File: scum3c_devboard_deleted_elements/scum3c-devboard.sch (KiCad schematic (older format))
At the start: 9 parts, among them U9AB1 MPU-9250

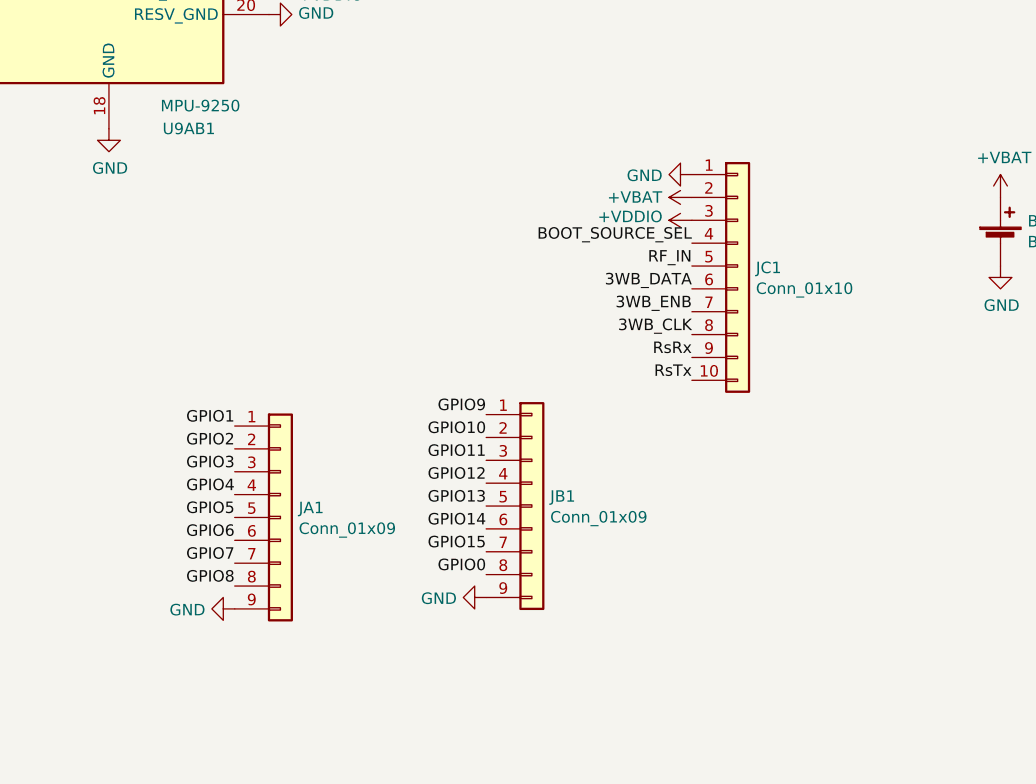
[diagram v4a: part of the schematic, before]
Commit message: shrink to 30mm square
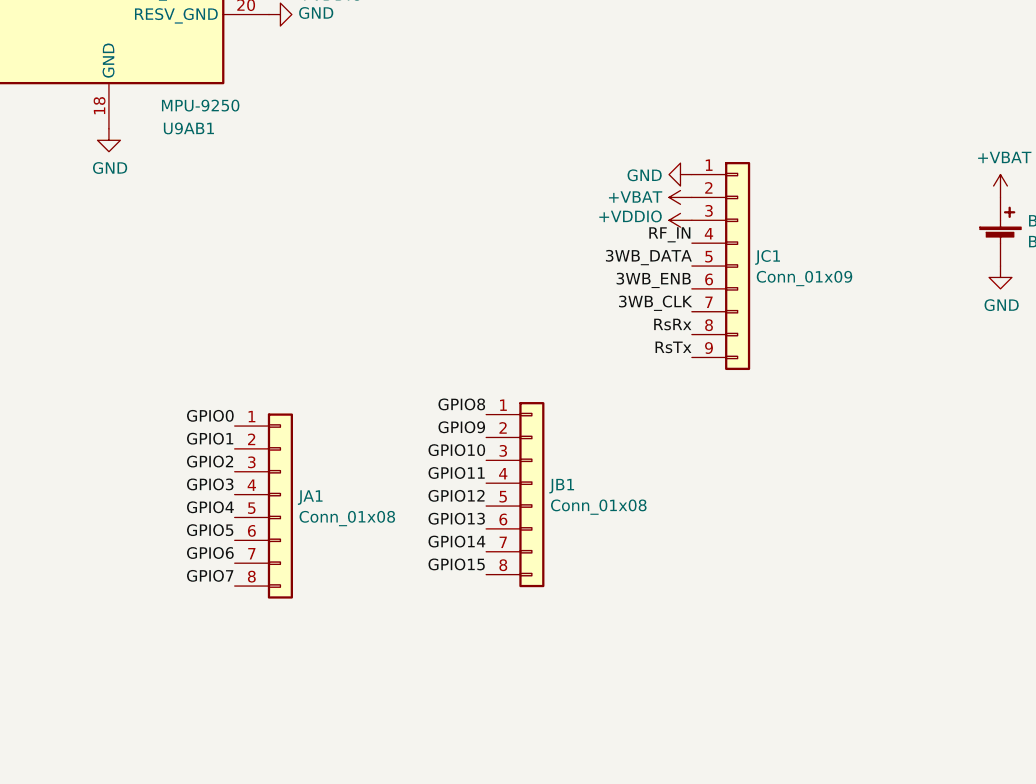
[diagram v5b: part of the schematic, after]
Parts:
- removed JA1, JB1: Conn_01x09, Connector_PinHeader_2.54mm:PinHeader_1x09_P2.54mm_Vertical, symbol Connector_Generic:Conn_01x09
- removed JC1: Conn_01x10, Connector_PinHeader_2.54mm:PinHeader_1x10_P2.54mm_Vertical, symbol Connector_Generic:Conn_01x10
- added JA1, JB1: Conn_01x08, Connector_PinHeader_2.54mm:PinHeader_1x08_P2.54mm_Vertical, symbol Connector_Generic:Conn_01x08
- added JC1: Conn_01x09, Connector_PinHeader_2.54mm:PinHeader_1x09_P2.54mm_Vertical, symbol Connector_Generic:Conn_01x09
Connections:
- net +VBAT: now also JC1.2 (Pin_2)
- net +VDDIO: now also JC1.3 (Pin_3)
- net 3WB_CLK: now also JC1.7 (Pin_7)
- net 3WB_DATA: now also JC1.5 (Pin_5)
- net 3WB_ENB: now also JC1.6 (Pin_6)
- net GND: now also JC1.1 (Pin_1)
- net GPIO0: now also JA1.1 (Pin_1)
- net GPIO1: now also JA1.2 (Pin_2)
- net GPIO10: now also JB1.3 (Pin_3)
- net GPIO11: now also JB1.4 (Pin_4)
- net GPIO12: now also JB1.5 (Pin_5)
- net GPIO13: now also JB1.6 (Pin_6)
- net GPIO14: now also JB1.7 (Pin_7)
- net GPIO15: now also JB1.8 (Pin_8)
- net GPIO2: now also JA1.3 (Pin_3)
- net GPIO3: now also JA1.4 (Pin_4)
- net GPIO4: now also JA1.5 (Pin_5)
- net GPIO5: now also JA1.6 (Pin_6)
- net GPIO6: now also JA1.7 (Pin_7)
- net GPIO7: now also JA1.8 (Pin_8)
- net GPIO8: now also JB1.1 (Pin_1)
- net GPIO9: now also JB1.2 (Pin_2)
- net RF_IN: now also JC1.4 (Pin_4)
- net RsRx: now also JC1.8 (Pin_8)
- net RsTx: now also JC1.9 (Pin_9)
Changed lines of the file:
@@
 	1    0    0    -1
 $EndComp
+Text Label 3550 4500 2    50   ~ 0
+GPIO10
+Text Label 3550 4700 2    50   ~ 0
+GPIO12
+Text Label 3550 4900 2    50   ~ 0
+GPIO14
+Text Label 3550 5000 2    50   ~ 0
+GPIO15
 Text Label 3550 4400 2    50   ~ 0
-GPIO10
+GPIO9
+Text Label 2450 4350 2    50   ~ 0
+GPIO0
+Text Label 3550 4800 2    50   ~ 0
+GPIO13
 Text Label 3550 4600 2    50   ~ 0
-GPIO12
-Text Label 3550 4800 2    50   ~ 0
-GPIO14
-Text Label 3550 4900 2    50   ~ 0
-GPIO15
-$Comp
-L power:GND #PWR0111
-U 1 1 5F3EC8B2
-P 2450 5150
-F 0 "#PWR0111" H 2450 4900 50  0001 C CNN
-F 1 "GND" V 2455 5022 50  0000 R CNN
-F 2 "" H 2450 5150 50  0001 C CNN
-F 3 "" H 2450 5150 50  0001 C CNN
-	1    2450 5150
-	0    1    1    0
-$EndComp
-Text Label 3550 4300 2    50   ~ 0
-GPIO9
-Text Label 3550 5000 2    50   ~ 0
-GPIO0
-Text Label 3550 4700 2    50   ~ 0
-GPIO13
-Text Label 3550 4500 2    50   ~ 0
 GPIO11
-$Comp
-L power:GND #PWR0112
-U 1 1 5F3ED1BB
-P 3550 5100
-F 0 "#PWR0112" H 3550 4850 50  0001 C CNN
-F 1 "GND" V 3555 4972 50  0000 R CNN
-F 2 "" H 3550 5100 50  0001 C CNN
-F 3 "" H 3550 5100 50  0001 C CNN
-	1    3550 5100
-	0    1    1    0
-$EndComp
 $Comp
 L power:PWR_FLAG #FLG0101
@@
 	0    -1   -1   0
 $EndComp
-Text Label 4450 3550 2    50   ~ 0
-BOOT_SOURCE_SEL
 $Comp
 L draft1library:+VDDIO #PWR?
@@
 Text Label 9400 3250 0    50   ~ 0
 BOOT_SOURCE_SEL
-$Comp
-L Connector_Generic:Conn_01x10 JC1
-U 1 1 5F7BC634
-P 4650 3650
-F 0 "JC1" H 4730 3642 50  0000 L CNN
-F 1 "Conn_01x10" H 4730 3551 50  0000 L CNN
-F 2 "Connector_PinHeader_2.54mm:PinHeader_1x10_P2.54mm_Vertical" H 4650 3650 50  0001 C CNN
-F 3 "~" H 4650 3650 50  0001 C CNN
-	1    4650 3650
-	1    0    0    -1
-$EndComp
+Text Label 2450 4650 2    50   ~ 0
+GPIO3
+Text Label 2450 4850 2    50   ~ 0
+GPIO5
+Text Label 2450 5050 2    50   ~ 0
+GPIO7
+Text Label 2450 4450 2    50   ~ 0
+GPIO1
 Text Label 2450 4550 2    50   ~ 0
-GPIO3
+GPIO2
 Text Label 2450 4750 2    50   ~ 0
-GPIO5
+GPIO4
 Text Label 2450 4950 2    50   ~ 0
-GPIO7
-Text Label 2450 4350 2    50   ~ 0
-GPIO1
-Text Label 2450 4450 2    50   ~ 0
-GPIO2
-Text Label 2450 4650 2    50   ~ 0
-GPIO4
-Text Label 2450 4850 2    50   ~ 0
 GPIO6
-Text Label 2450 5050 2    50   ~ 0
+Text Label 3550 4300 2    50   ~ 0
 GPIO8
 Text Label 9400 1500 0    50   ~ 0
@@
 Text Label 8550 3050 2    50   ~ 0
 RsTx
-$Comp
-L Connector_Generic:Conn_01x09 JA1
-U 1 1 5F7CC956
-P 2650 4750
-F 0 "JA1" H 2730 4792 50  0000 L CNN
-F 1 "Conn_01x09" H 2730 4701 50  0000 L CNN
-F 2 "Connector_PinHeader_2.54mm:PinHeader_1x09_P2.54mm_Vertical" H 2650 4750 50  0001 C CNN
-F 3 "~" H 2650 4750 50  0001 C CNN
-	1    2650 4750
-	1    0    0    -1
-$EndComp
-$Comp
-L Connector_Generic:Conn_01x09 JB1
-U 1 1 5F7CF946
-P 3750 4700
-F 0 "JB1" H 3830 4742 50  0000 L CNN
-F 1 "Conn_01x09" H 3830 4651 50  0000 L CNN
-F 2 "Connector_PinHeader_2.54mm:PinHeader_1x09_P2.54mm_Vertical" H 3750 4700 50  0001 C CNN
-F 3 "~" H 3750 4700 50  0001 C CNN
-	1    3750 4700
-	1    0    0    -1
-$EndComp
 $Comp
 L power:GND #PWR0124
@@
 	0    1    1    0
 $EndComp
+Text Label 4450 3950 2    50   ~ 0
+RsRx
 Text Label 4450 4050 2    50   ~ 0
-RsRx
-Text Label 4450 4150 2    50   ~ 0
 RsTx
-Text Label 4450 3950 2    50   ~ 0
+Text Label 4450 3850 2    50   ~ 0
 3WB_CLK
-Text Label 4450 3850 2    50   ~ 0
+Text Label 4450 3750 2    50   ~ 0
 3WB_ENB
-Text Label 4450 3750 2    50   ~ 0
+Text Label 4450 3650 2    50   ~ 0
 3WB_DATA
-Text Label 4450 3650 2    50   ~ 0
+Text Label 4450 3550 2    50   ~ 0
 RF_IN
+$Comp
+L Connector_Generic:Conn_01x08 JA1
+U 1 1 5F7FC97F
+P 2650 4650
+F 0 "JA1" H 2730 4642 50  0000 L CNN
+F 1 "Conn_01x08" H 2730 4551 50  0000 L CNN
+F 2 "Connector_PinHeader_2.54mm:PinHeader_1x08_P2.54mm_Vertical" H 2650 4650 50  0001 C CNN
+F 3 "~" H 2650 4650 50  0001 C CNN
+	1    2650 4650
+	1    0    0    -1
+$EndComp
+$Comp
+L Connector_Generic:Conn_01x08 JB1
+U 1 1 5F7FD7A2
+P 3750 4600
+F 0 "JB1" H 3830 4592 50  0000 L CNN
+F 1 "Conn_01x08" H 3830 4501 50  0000 L CNN
+F 2 "Connector_PinHeader_2.54mm:PinHeader_1x08_P2.54mm_Vertical" H 3750 4600 50  0001 C CNN
+F 3 "~" H 3750 4600 50  0001 C CNN
+	1    3750 4600
+	1    0    0    -1
+$EndComp
+$Comp
+L Connector_Generic:Conn_01x09 JC1
+U 1 1 5F804045
+P 4650 3650
+F 0 "JC1" H 4730 3692 50  0000 L CNN
+F 1 "Conn_01x09" H 4730 3601 50  0000 L CNN
+F 2 "Connector_PinHeader_2.54mm:PinHeader_1x09_P2.54mm_Vertical" H 4650 3650 50  0001 C CNN
+F 3 "~" H 4650 3650 50  0001 C CNN
+	1    4650 3650
+	1    0    0    -1
+$EndComp
 $EndSCHEMATC

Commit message: changed header size
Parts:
- JA1, JB1: footprint Connector_PinHeader_2.54mm:PinHeader_1x08_P2.54mm_Vertical -> Connector_PinHeader_1.27mm:PinHeader_1x08_P1.27mm_Vertical
- JC1: footprint Connector_PinHeader_2.54mm:PinHeader_1x09_P2.54mm_Vertical -> Connector_PinHeader_1.27mm:PinHeader_1x09_P1.27mm_Vertical
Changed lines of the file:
@@
 F 0 "JA1" H 2730 4642 50  0000 L CNN
 F 1 "Conn_01x08" H 2730 4551 50  0000 L CNN
-F 2 "Connector_PinHeader_2.54mm:PinHeader_1x08_P2.54mm_Vertical" H 2650 4650 50  0001 C CNN
+F 2 "Connector_PinHeader_1.27mm:PinHeader_1x08_P1.27mm_Vertical" H 2650 4650 50  0001 C CNN
 F 3 "~" H 2650 4650 50  0001 C CNN
 	1    2650 4650
@@
 F 0 "JB1" H 3830 4592 50  0000 L CNN
 F 1 "Conn_01x08" H 3830 4501 50  0000 L CNN
-F 2 "Connector_PinHeader_2.54mm:PinHeader_1x08_P2.54mm_Vertical" H 3750 4600 50  0001 C CNN
+F 2 "Connector_PinHeader_1.27mm:PinHeader_1x08_P1.27mm_Vertical" H 3750 4600 50  0001 C CNN
 F 3 "~" H 3750 4600 50  0001 C CNN
 	1    3750 4600
@@
 F 0 "JC1" H 4730 3692 50  0000 L CNN
 F 1 "Conn_01x09" H 4730 3601 50  0000 L CNN
-F 2 "Connector_PinHeader_2.54mm:PinHeader_1x09_P2.54mm_Vertical" H 4650 3650 50  0001 C CNN
+F 2 "Connector_PinHeader_1.27mm:PinHeader_1x09_P1.27mm_Vertical" H 4650 3650 50  0001 C CNN
 F 3 "~" H 4650 3650 50  0001 C CNN
 	1    4650 3650
